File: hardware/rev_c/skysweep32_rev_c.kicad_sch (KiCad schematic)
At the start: 63 parts, among them J1 USB4105-GF-A, J2 Molex 104031-0811, J3 OLED STEMMA QT, J4 OPTIONAL VIBRATION MOTOR, J5 SUB-GHZ SMA, Q1 AO3400A, Q2 AO3400A, SW1 RESET, SW2 BOOT, SW3 USER, U1 ESP32-S3-WROOM-1-N8, U2 USBLC6-2SC6, U3 AP63203WU-7

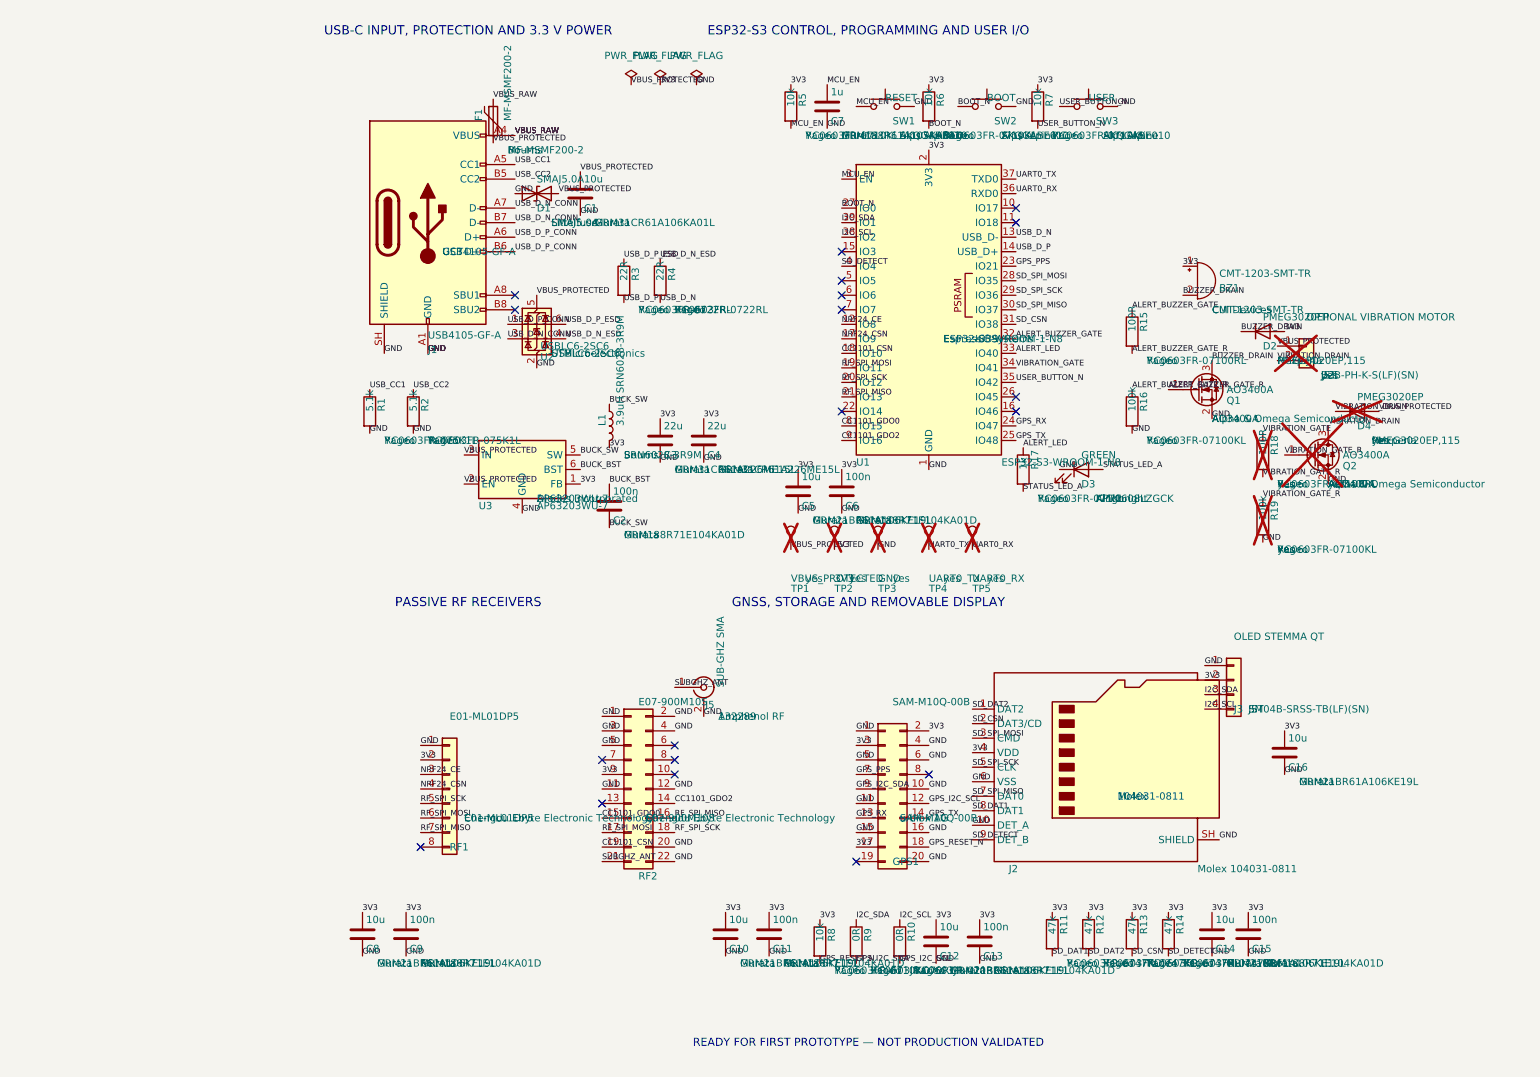
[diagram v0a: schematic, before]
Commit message: fix(hardware): close Rev C prototype review gaps
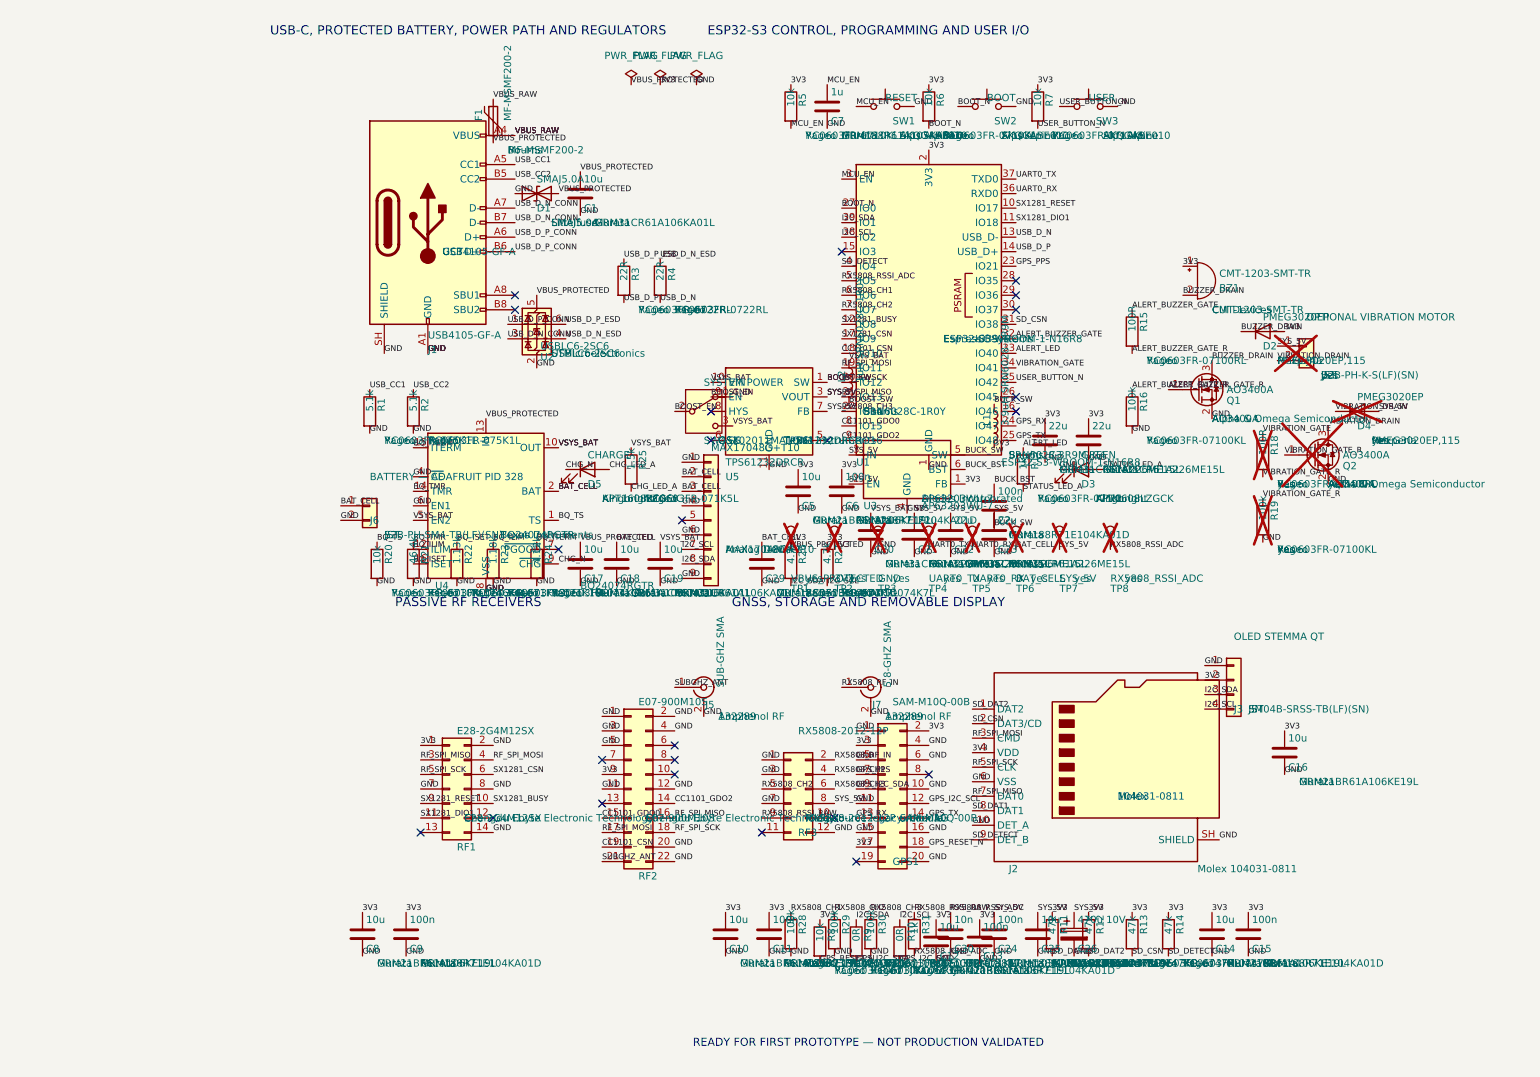
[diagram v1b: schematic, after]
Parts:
- removed RF1: E01-ML01DP5, SkySweep32RevC:Module_Ebyte_E01_ML01DP5, symbol Connector_Generic:Conn_01x08
- added C17, C18, C19: 10u, Capacitor_SMD:C_1206_3216Metric, symbol Device:C
- added C20, C21, C22, C23: 22u, Capacitor_SMD:C_1206_3216Metric, symbol Device:C
- added C24, C29: 100n, Capacitor_SMD:C_0603_1608Metric, symbol Device:C
- added C25: 10u, Capacitor_SMD:C_0805_2012Metric, symbol Device:C
- added C26: 470u 10V, Capacitor_SMD:CP_Elec_10x10, symbol Device:C_Polarized
- added C30: 10n, Capacitor_SMD:C_0603_1608Metric, symbol Device:C
- added D5: CHARGE, LED_SMD:LED_0603_1608Metric, symbol Device:LED
- added J6: BATTERY — ADAFRUIT PID 328, Connector_JST:JST_PH_S2B-PH-SM4-TB_1x02-1MP_P2.00mm_Horizontal, symbol Connector_Generic:Conn_01x02
- added J7: 5.8-GHZ SMA, Connector_Coaxial:SMA_Amphenol_132289_EdgeMount, symbol Connector:Conn_Coaxial
- added L2: 1uH SRN6028C-1R0Y, Inductor_SMD:L_Bourns-SRN6028, symbol Device:L
- added R20: 10k, Resistor_SMD:R_0603_1608Metric, symbol Device:R
- added R21: 46.4k, Resistor_SMD:R_0603_1608Metric, symbol Device:R
- added R22: 1.13k, Resistor_SMD:R_0603_1608Metric, symbol Device:R
- added R23: 1.18k, Resistor_SMD:R_0603_1608Metric, symbol Device:R
- added R24: 4.12k, Resistor_SMD:R_0603_1608Metric, symbol Device:R
- added R25: 1.5k, Resistor_SMD:R_0603_1608Metric, symbol Device:R
- added R26, R27: 4.7k, Resistor_SMD:R_0603_1608Metric, symbol Device:R
- added R28, R29, R30: 100k, Resistor_SMD:R_0603_1608Metric, symbol Device:R
- added R31: 1k, Resistor_SMD:R_0603_1608Metric, symbol Device:R
- added RF1: E28-2G4M12SX, SkySweep32RevC:Module_Ebyte_E28_2G4M12SX, symbol Connector_Generic:Conn_02x07_Odd_Even
- added RF3: RX5808-2012-12P, SkySweep32RevC:Module_RX5808_2012_12P, symbol Connector_Generic:Conn_02x06_Odd_Even
- added SW4: SYSTEM POWER, Button_Switch_THT:SW_Slide_SPDT_Angled_CK_OS102011MA1Q, symbol Switch:SW_SPDT
- added TP6: BAT_CELL, TestPoint:TestPoint_Pad_D1.0mm, symbol Connector:TestPoint
- added TP7: SYS_5V, TestPoint:TestPoint_Pad_D1.0mm, symbol Connector:TestPoint
- added TP8: RX5808_RSSI_ADC, TestPoint:TestPoint_Pad_D1.0mm, symbol Connector:TestPoint
- added U4: BQ24074RGTR, Package_DFN_QFN:VQFN-16-1EP_3x3mm_P0.5mm_EP1.6x1.6mm, symbol Battery_Management:BQ24074RGT
- added U5: TPS61232DRCR, Package_SON:Texas_S-PVSON-N10_ThermalVias, symbol Regulator_Switching:TPS61230DRC
- added U6: MAX17048G+T10, Package_DFN_QFN:DFN-8-1EP_2x2mm_P0.5mm_EP0.9x1.3mm, symbol Connector_Generic:Conn_01x09
- U1: value ESP32-S3-WROOM-1-N8 -> ESP32-S3-WROOM-1-N16R8; MPN ESP32-S3-WROOM-1-N8 -> ESP32-S3-WROOM-1-N16R8
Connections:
- net 3V3: now also R26.1, R27.1, RF1.1 (Pin_1)
- net GND: now also C17.2, C18.2, C19.2, C20.2, C21.2, C22.2, C23.2, C24.2, C25.2, C26.2, C29.2, C30.2, J6.2 (Pin_2), J7.2 (Ext), R20.2, R21.2, R22.2, R23.2, R24.2, R28.2, R29.2, R30.2, RF1.14 (Pin_14), RF1.2 (Pin_2), RF1.7 (Pin_7), RF1.8 (Pin_8), RF3.1 (Pin_1), RF3.12 (Pin_12), RF3.3 (Pin_3), RF3.7 (Pin_7), SW4.1 (A), U4.17 (VSS), U4.4 (~{CE}), U4.6 (EN1), U4.8 (VSS), U5.11 (GND), U6.1 (Pin_1), U6.4 (Pin_4), U6.6 (Pin_6), U6.9 (Pin_9)
- net I2C_SCL: now also R27.2, U6.7 (Pin_7)
- net I2C_SDA: now also R26.2, U6.8 (Pin_8)
- net RF_SPI_MISO: now also J2.7 (DAT0), RF1.3 (Pin_3)
- net RF_SPI_MOSI: now also J2.3 (CMD), RF1.4 (Pin_4)
- net RF_SPI_SCK: now also J2.5 (CLK), RF1.5 (Pin_5)
- net VBUS_PROTECTED: now also C17.1, U4.13 (IN); no longer D4.2 (A), J4.1 (Pin_1), U3.2 (EN), U3.3 (IN)
- net SX1281_RESET: now reaches U1.10 (IO17)
- net SX1281_RESET: now also RF1.9 (Pin_9)
- net SX1281_DIO1: now reaches U1.11 (IO18)
- net SX1281_DIO1: now also RF1.11 (Pin_11)
- net RX5808_CH3: now reaches U1.22 (IO14)
- net RX5808_CH3: now also R30.1, RF3.6 (Pin_6)
- net RX5808_RSSI_ADC: now reaches U1.5 (IO5)
- net RX5808_RSSI_ADC: now also C30.1, R31.2, TP8.1
- net RX5808_CH1: now reaches U1.6 (IO6)
- net RX5808_CH1: now also R28.1, RF3.4 (Pin_4)
- net RX5808_CH2: now reaches U1.7 (IO7)
- net RX5808_CH2: now also R29.1, RF3.5 (Pin_5)
- net NRF24_CE renamed SX1281_BUSY
- net SX1281_BUSY: now also RF1.10 (Pin_10)
- net NRF24_CSN renamed SX1281_CSN
- net SX1281_CSN: now also RF1.6 (Pin_6)
- net SD_SPI_MISO: no longer names the net of U1.30 (IO37)
- net SD_SPI_MISO: no longer J2.7 (DAT0)
- net SD_SPI_MOSI: no longer names the net of U1.28 (IO35)
- net SD_SPI_MOSI: no longer J2.3 (CMD)
- net SD_SPI_SCK: no longer names the net of U1.29 (IO36)
- net SD_SPI_SCK: no longer J2.5 (CLK)
- new net BAT_CELL: C18.1, C29.1, J6.1 (Pin_1), TP6.1, U4.2 (BAT), U4.3 (BAT), U6.2 (Pin_2), U6.3 (Pin_3)
- new net BOOST_EN: SW4.2 (B), U5.9 (EN)
- new net BOOST_SW: L2.2, U5.1 (SW), U5.2 (SW)
- new net BQ_ILIM: R23.1, U4.12 (ILIM)
- new net BQ_ISET: R22.1, U4.16 (ISET)
- new net BQ_ITERM: R24.1, U4.15 (ITERM)
- new net BQ_TMR: R21.1, U4.14 (TMR)
- new net BQ_TS: R20.1, U4.1 (TS)
- new net CHG_LED_A: D5.2 (A), R25.2
- new net CHG_N: D5.1 (K), U4.9 (~{CHG})
- new net RX5808_RF_IN: J7.1 (In), RF3.2 (Pin_2)
- new net RX5808_RSSI_RAW: R31.1, RF3.9 (Pin_9)
- new net SYS_5V: C21.1, C22.1, C23.1, C24.1, C25.1, C26.1, D4.2 (A), J4.1 (Pin_1), RF3.8 (Pin_8), TP7.1, U3.2 (EN), U3.3 (IN), U5.3 (VOUT), U5.4 (VOUT), U5.7 (FB)
- new net VSYS_BAT: C19.1, C20.1, L2.1, R25.1, SW4.3 (C), U4.10 (OUT), U4.11 (OUT), U4.5 (EN2), U5.10 (VIN)
- no-connect marks 19 -> 24
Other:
- note added: "USB-C, PROTECTED BATTERY, POWER PATH AND REGULATORS"
- note removed: "USB-C INPUT, PROTECTION AND 3.3 V POWER"

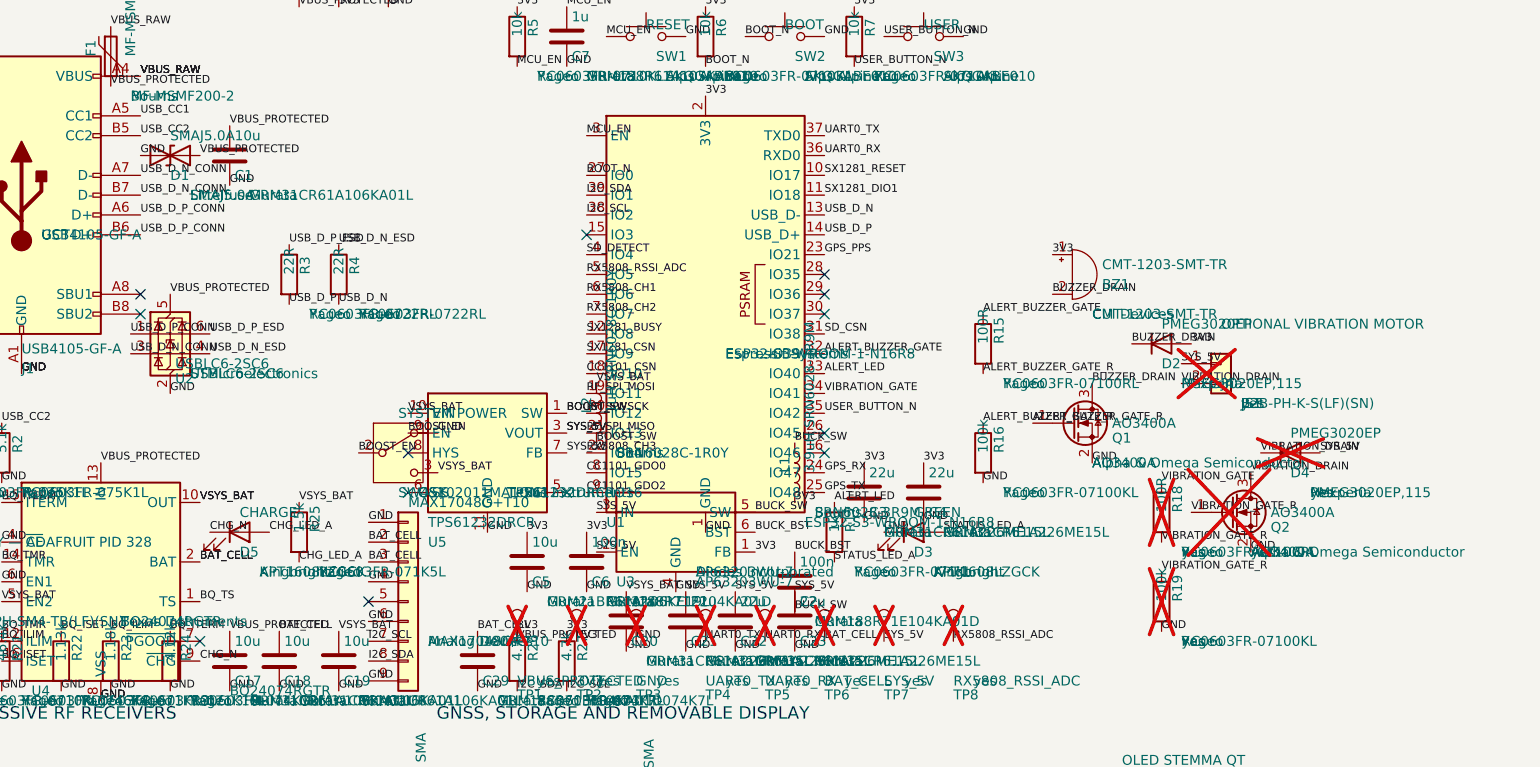
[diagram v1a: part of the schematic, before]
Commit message: fix(hardware): correct Rev C electrical integration
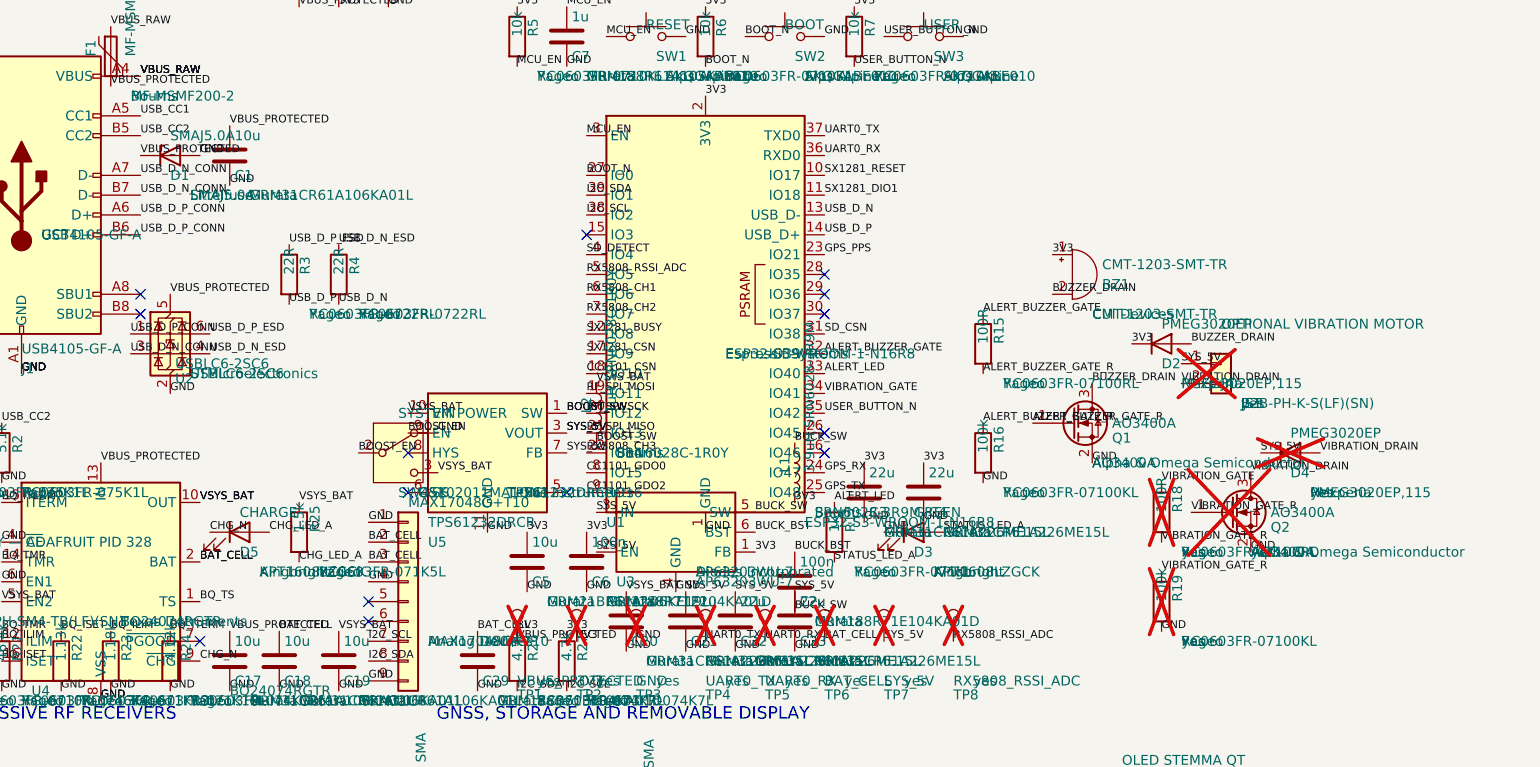
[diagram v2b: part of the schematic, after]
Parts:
- removed D1: SMAJ5.0A, Diode_SMD:D_SMA, symbol Device:D_TVS
- added D1: SMAJ5.0A, Diode_SMD:D_SMA, symbol Device:D_Zener
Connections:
- net 3V3: now also D2.1 (K); no longer D2.2 (A)
- net BUZZER_DRAIN: now also D2.2 (A); no longer D2.1 (K)
- net GND: now also D1.2 (A); no longer U6.6 (Pin_6)
- net SYS_5V: now also D4.1 (K); no longer D4.2 (A)
- net VBUS_PROTECTED: now also D1.1 (K)
- net VIBRATION_DRAIN: now also D4.2 (A); no longer D4.1 (K)
- no-connect marks 24 -> 25
